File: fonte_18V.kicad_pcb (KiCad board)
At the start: 2 copper layers, 24 parts, among them J1 RJ45_Shielded, Q1 Q_NMOS_GSD, U1 LMR16030

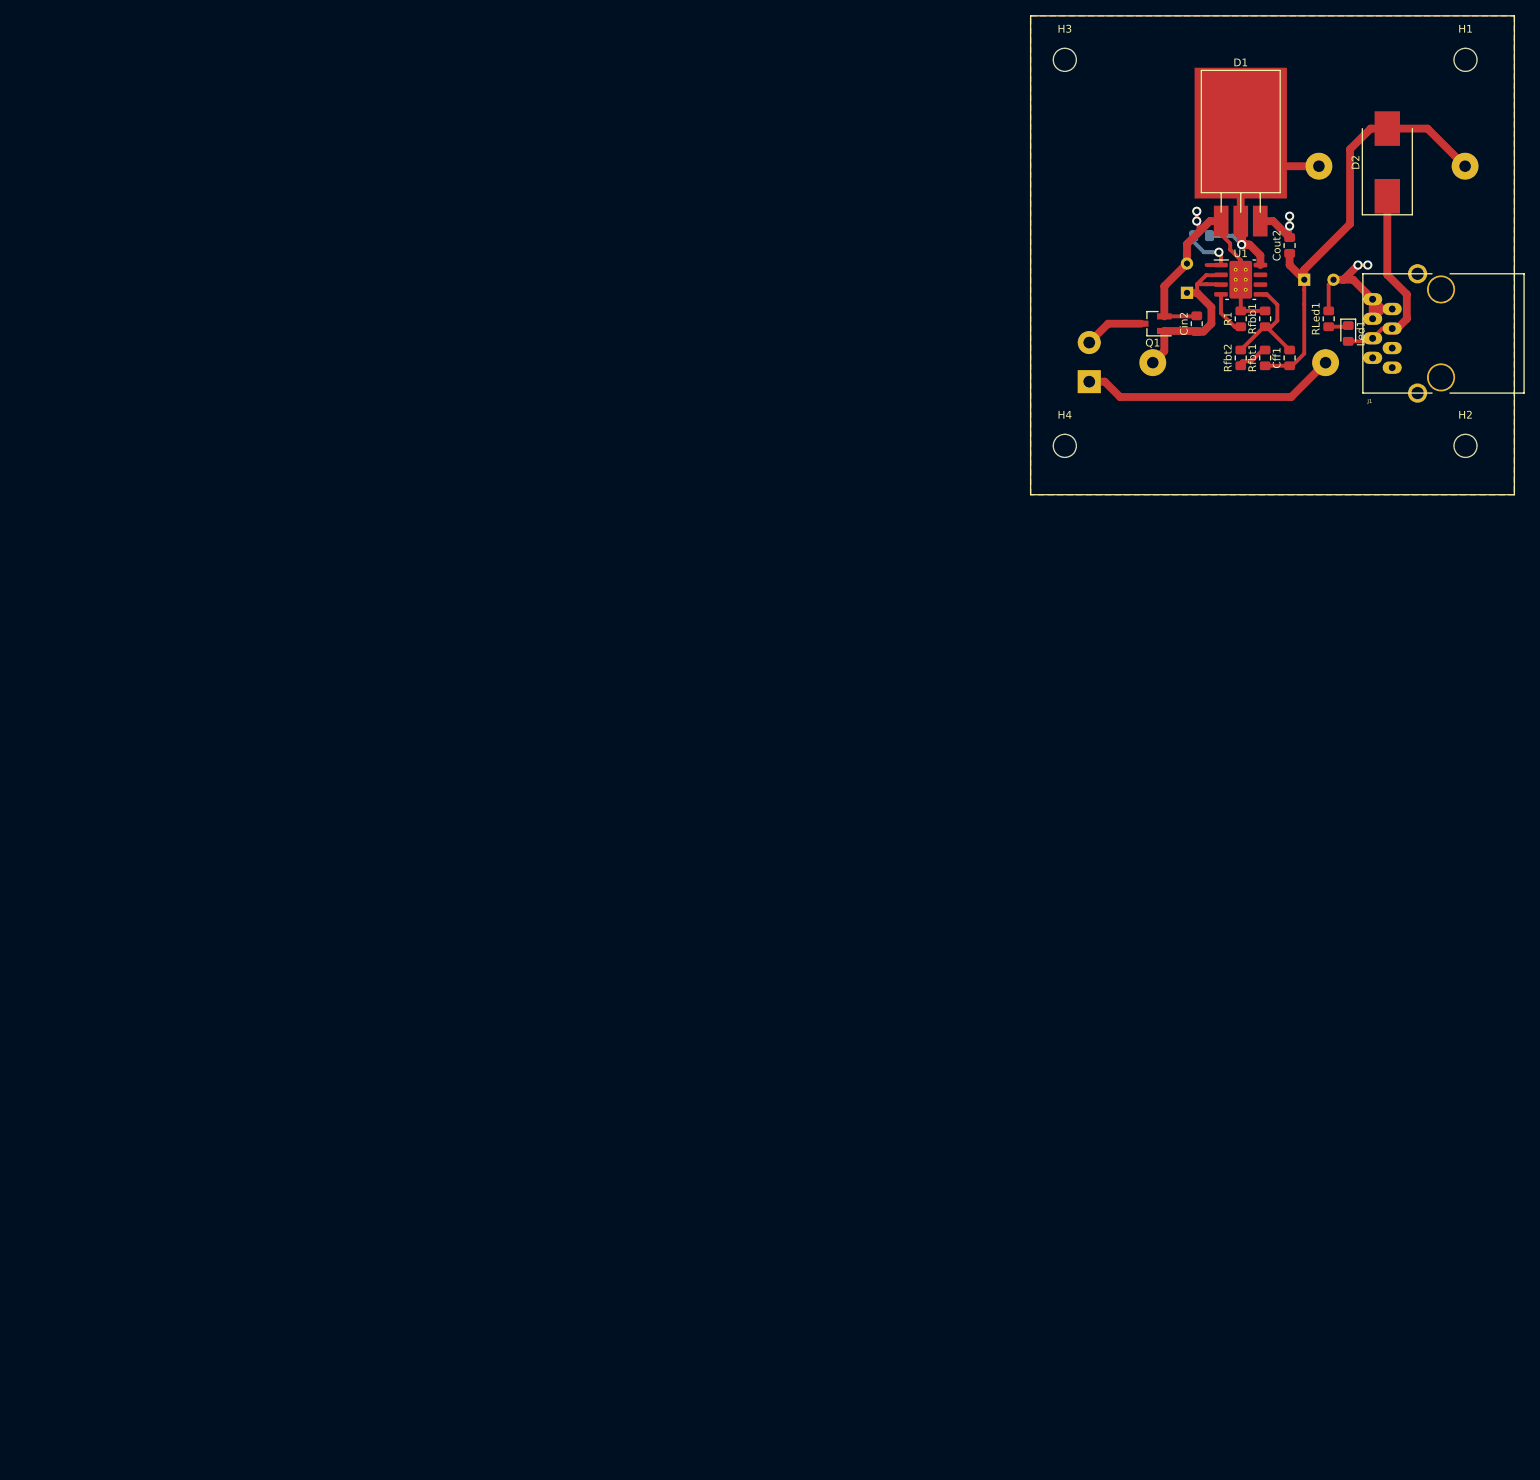
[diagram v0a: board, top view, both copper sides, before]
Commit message: Conectores rj45 adicionados, trilhas melhoradas, acabamentos gerais
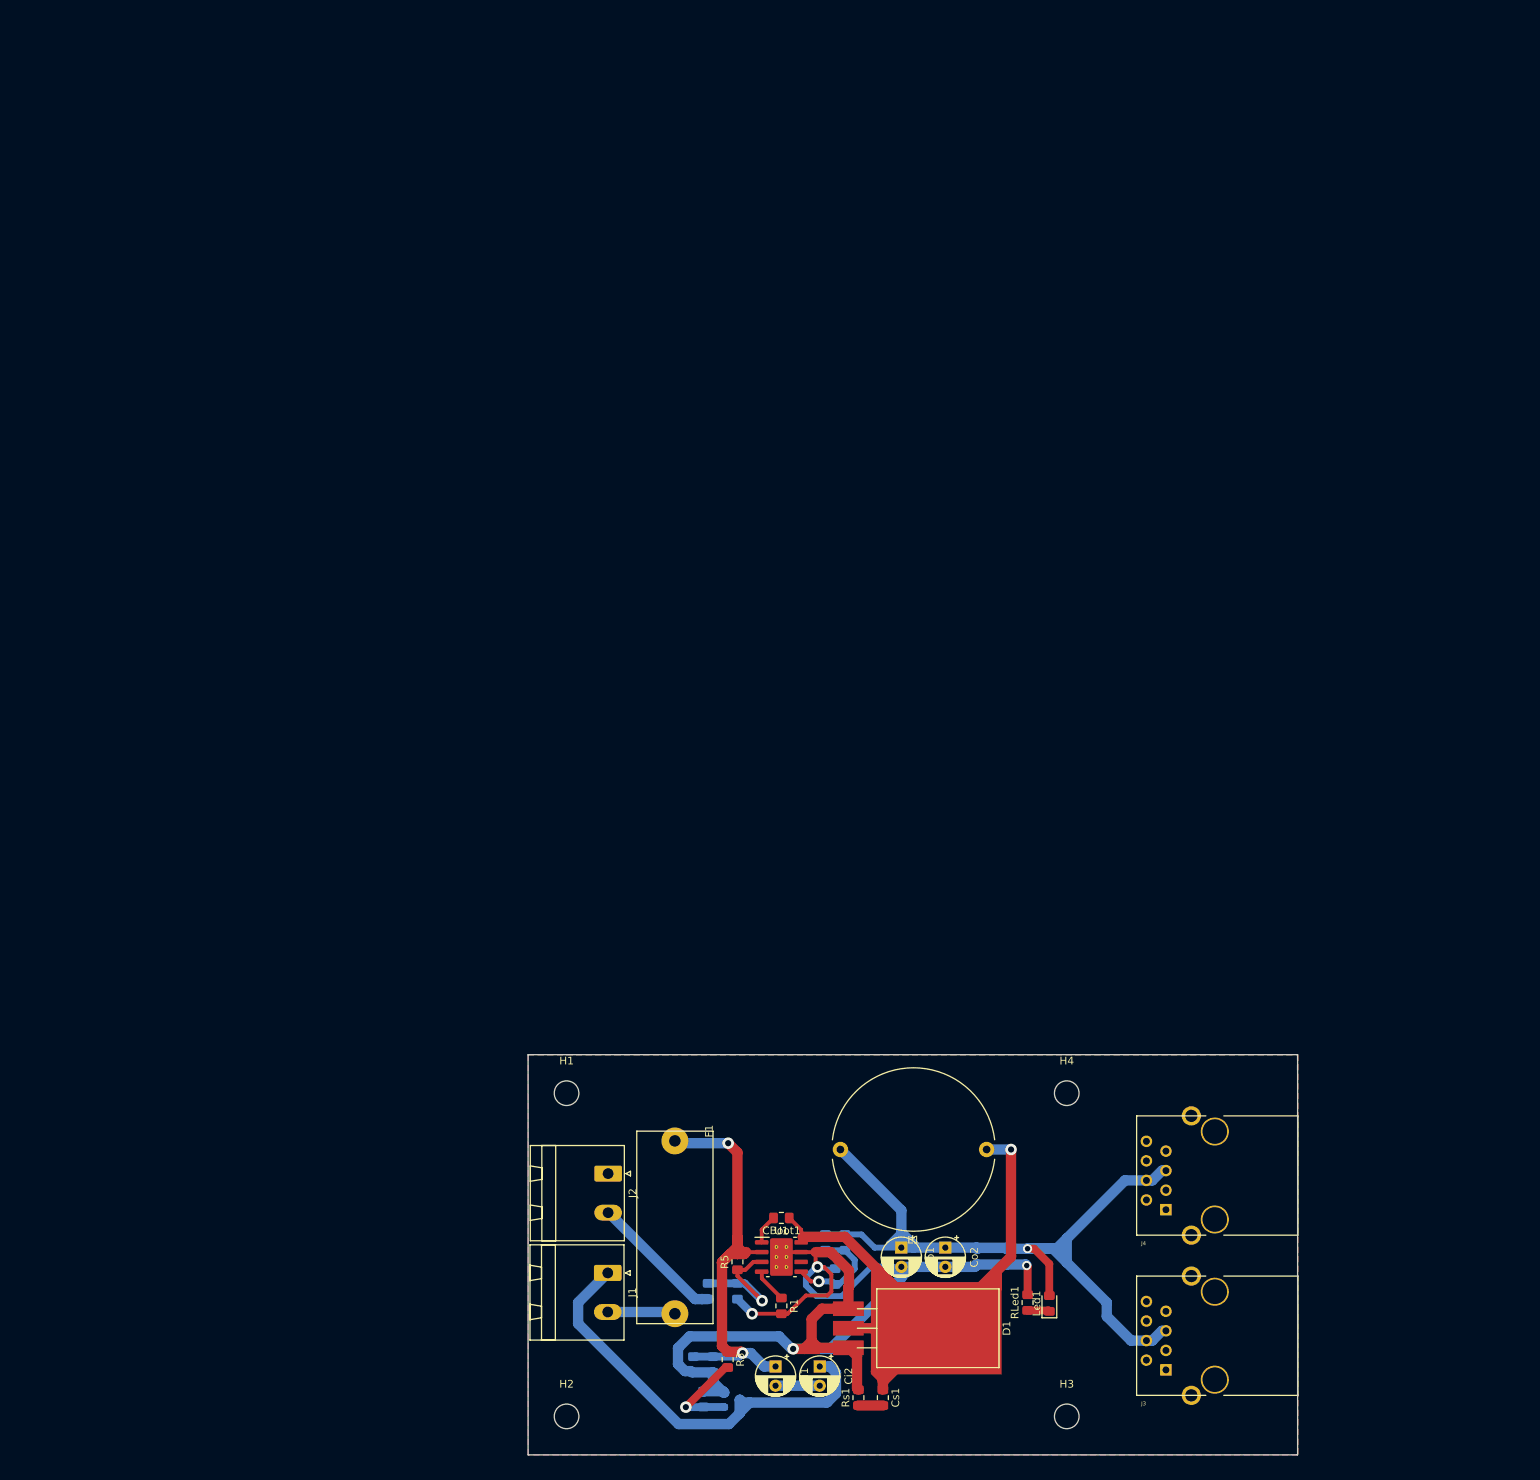
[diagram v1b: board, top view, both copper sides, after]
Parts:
- removed Cin1, Cout1: 100uF, Capacitor_THT:CP_Radial_D8.0mm_P3.80mm
- removed Cout2: 100nF, Capacitor_SMD:C_0805_2012Metric_Pad1.15x1.40mm_HandSolder
- removed D2: SS35, Diode_SMD:D_SMC_Handsoldering
- removed Rfbt1: 5k6, Resistor_SMD:R_0805_2012Metric_Pad1.15x1.40mm_HandSolder
- removed battery1: 21.5<+VBAT<55V1, TerminalBlock:TerminalBlock_bornier-2_P5.08mm
- added Ci1: 10u, Capacitor_THT:CP_Radial_D5.0mm_P2.50mm, F.Cu at (121.2, 175.5)
- added Ci2: 10u, Capacitor_THT:CP_Radial_D5.0mm_P2.50mm, F.Cu at (126.9, 175.5)
- added Cin3: 100nF, Capacitor_SMD:C_0805_2012Metric_Pad1.15x1.40mm_HandSolder, B.Cu at (110.5, 175.3)
- added Co1: 47u, Capacitor_THT:CP_Radial_D5.0mm_P2.50mm, F.Cu at (137.5, 160.1)
- added Co2: 47u, Capacitor_THT:CP_Radial_D5.0mm_P2.50mm, F.Cu at (143.2, 160.1)
- added Co3: o.1u, Capacitor_SMD:C_0805_2012Metric_Pad1.15x1.40mm_HandSolder, B.Cu at (151.2, 161.2)
- added Co4: 0.1u, Capacitor_SMD:C_0805_2012Metric_Pad1.15x1.40mm_HandSolder, B.Cu at (147.4, 161.2)
- added Cs1: 100n, Capacitor_SMD:C_0805_2012Metric_Pad1.15x1.40mm_HandSolder, F.Cu at (135.1, 179.6)
- added J2: MSTBA, Connector_Phoenix_MSTB:PhoenixContact_MSTBA_2,5_2-G-5,08_1x02_P5.08mm_Horizontal, F.Cu at (99.4, 150.4)
- added J3: RJ45_Shielded, MFP19RJ45:RJ45_YH59_01, F.Cu at (171.9, 176.0)
- added J4: RJ45_Shielded, MFP19RJ45:RJ45_YH59_01, F.Cu at (171.9, 155.2)
- added R2: 100, Resistor_SMD:R_0805_2012Metric_Pad1.15x1.40mm_HandSolder, B.Cu at (112.4, 165.7)
- added R3: 220K, Resistor_SMD:R_0805_2012Metric_Pad1.15x1.40mm_HandSolder, F.Cu at (114.9, 174.6)
- added R4: 100K, Resistor_SMD:R_0805_2012Metric_Pad1.15x1.40mm_HandSolder, B.Cu at (111.8, 179.8)
- added R5: 10K, Resistor_SMD:R_0805_2012Metric_Pad1.15x1.40mm_HandSolder, F.Cu at (116.2, 161.9)
- added R6: NA, Resistor_SMD:R_0805_2012Metric_Pad1.15x1.40mm_HandSolder, B.Cu at (116.2, 165.7)
- added Rs1: 2k2, Resistor_SMD:R_0805_2012Metric_Pad1.15x1.40mm_HandSolder, F.Cu at (131.9, 179.6)
- CBoot1, L1: moved to F.Cu
- Cff1: value 33.0pF -> na; moved to B.Cu
- Cin2: moved to B.Cu
- F1: value Fuse -> 2A; moved to F.Cu
- H1, H2, H3, H4: footprint MountingHole:MountingHole_3mm -> MountingHole:MountingHole_3.2mm_M3
- J1: value RJ45_Shielded -> MSTBA; footprint KicadZeniteSolarLibrary18:RJ45_YH59_01 -> Connector_Phoenix_MSTB:PhoenixContact_MSTBA_2,5_2-G-5,08_1x02_P5.08mm_Horizontal
- Q1: value Q_NMOS_GSD -> Si2308CDS; footprint Package_TO_SOT_SMD:SOT-23_Handsoldering -> Package_TO_SOT_SMD:SOT-23; moved to B.Cu
- RLed1: value 750R -> 1k5
- Rfbb1: value 2k2 -> 8k2; moved to B.Cu
- Rfbt2: value 47k -> 230k; moved to B.Cu
- moved H1 178.0 mm to (94.0, 140.0)
- moved H3 176.3 mm to (159.0, 182.0)
- moved H2 171.9 mm to (94.0, 182.0)
- moved J1 155.7 mm to (99.4, 163.4), turned to 270 degrees
- moved Q1 150.2 mm to (115.5, 179.8), turned to 0 degrees
- moved D1 149.4 mm to (130.6, 168.0), turned to 270 degrees
- moved Cin2 149.2 mm to (113.0, 175.3), turned to 270 degrees
- moved R1 141.5 mm to (121.9, 167.6), turned to 270 degrees
- moved U1 140.3 mm to (121.9, 161.3)
- moved CBoot1 138.8 mm to (121.9, 156.2)
- moved Rfbb1 136.4 mm to (128.9, 163.8)
- moved L1 134.9 mm to (148.6, 147.3), turned to 180 degrees
- moved RLed1 133.7 mm to (153.9, 167.2)
- moved Led1 131.9 mm to (156.7, 167.3), turned to 90 degrees
- moved Cff1 128.6 mm to (130.2, 159.4), turned to 270 degrees
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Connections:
- net Net-(Cff1-Pad2) renamed /Feedback
- Cff1 pad 1: Net-(Cff1-Pad1) -> /CAN_18V
- Cin2 pad 1: Net-(Cin1-Pad1) -> Net-(Ci1-Pad1)
- F1 pad 1: Net-(Cin1-Pad1) -> Net-(Ci1-Pad1)
- J1 pad 1: Net-(J1-Pad1) -> Net-(Ci2-Pad1)
- J1 pad 2: Net-(J1-Pad2) -> Net-(F1-Pad2)
- L1 pad 2: Net-(Cff1-Pad1) -> /CAN_18V
- Led1 pad 2: /canbus_connector/CAN_18V -> /CAN_18V
- Q1 pad 1: Net-(Cin1-Pad1) -> Net-(Q1-Pad1)
- Q1 pad 3: Net-(Q1-Pad3) -> Net-(Ci2-Pad1)
- Rfbt2 pad 1: Net-(Rfbt1-Pad2) -> /CAN_18V
- U1 pad 2: Net-(Cin1-Pad1) -> Net-(Ci1-Pad1)
- U1 pad 3: Net-(Cin1-Pad1) -> Net-(R2-Pad1)
- U1 pad 6: Net-(U1-Pad6) -> (no net)
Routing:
- net /CAN_18V: track 0.00 -> 108.7 mm, vias 0 -> 1
- net GND: track 71.4 -> 159.8 mm, vias 6 -> 4
- net Net-(Ci1-Pad1): track 0.00 -> 61.3 mm, vias 0 -> 2
- net Net-(Cff1-Pad1): track 57.7 -> 0.00 mm
- net Net-(CBoot1-Pad1): track 41.2 -> 98.6 mm
- net Net-(Ci2-Pad1): track 0.00 -> 57.2 mm
- net /canbus_connector/CAN_18V: track 25.8 -> 0.00 mm
- net Net-(F1-Pad2): track 33.4 -> 8.81 mm
- net Net-(Cin1-Pad1): track 24.2 -> 0.00 mm
- net Net-(J2-Pad2): track 0.00 -> 17.6 mm
- net Net-(R2-Pad1): track 0.00 -> 16.9 mm, vias 0 -> 1
- net Net-(Q1-Pad1): track 0.00 -> 12.6 mm, vias 0 -> 1
- net Net-(Q1-Pad3): track 7.77 -> 0.00 mm
- net Net-(Ci1-Pad2): track 0.00 -> 5.74 mm
- net Net-(CBoot1-Pad2): track 8.29 -> 3.81 mm, vias 1 -> 0
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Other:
- board outline added: 100 x 52 mm

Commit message: atualizado
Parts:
- moved Cff1 66.6 mm to (63.6, 160.6)
- moved Ci2 66.6 mm to (60.3, 176.7)
- moved Co3 66.6 mm to (84.6, 162.4)
- moved Co4 66.6 mm to (80.8, 162.4)
- moved D1 66.6 mm to (64.0, 169.2)
- moved J2 66.6 mm to (32.8, 151.7)
- moved L1 66.6 mm to (82.0, 148.5)
- moved Led1 66.6 mm to (90.1, 168.5)
- moved Rfbt2 66.6 mm to (61.0, 160.6)
- moved Rs1 66.6 mm to (65.3, 180.8)
- moved CBoot1 66.6 mm to (55.3, 157.4)
- moved Ci1 66.6 mm to (54.6, 176.7)
- moved Cin2 66.6 mm to (46.4, 176.5)
- moved Cin3 66.6 mm to (43.9, 176.5)
- moved Co1 66.6 mm to (70.9, 161.3)
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
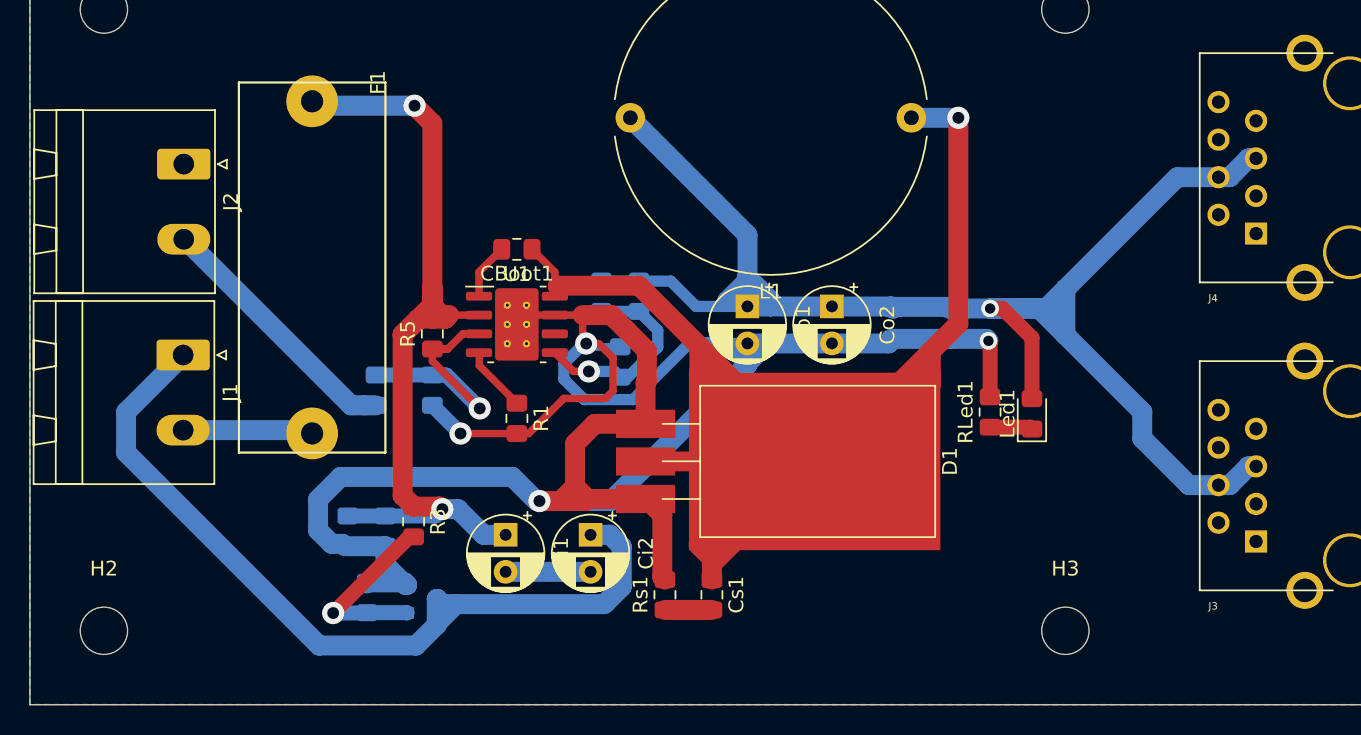
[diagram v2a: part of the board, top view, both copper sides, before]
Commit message: Pads reforçados, algumas pequenas correções de regras
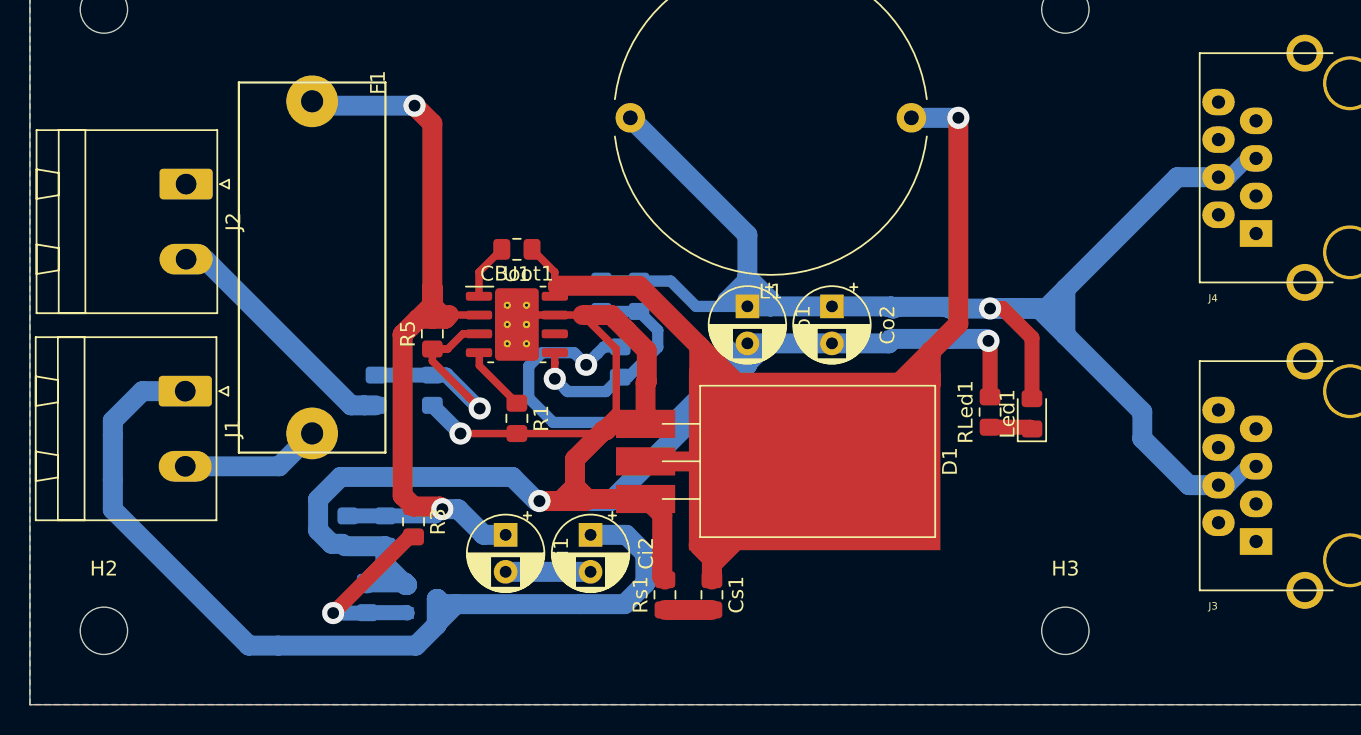
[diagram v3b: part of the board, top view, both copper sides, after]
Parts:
- moved J1 2.45 mm to (32.9, 167.0)
- moved J2 1.36 mm to (33.0, 153.0)
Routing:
- net GND: track 159.8 -> 167.3 mm
- net Net-(Ci2-Pad1): track 57.2 -> 62.8 mm
- net /Feedback: track 14.5 -> 15.8 mm
- net Net-(J2-Pad2): track 17.6 -> 16.9 mm
- net Net-(F1-Pad2): track 8.81 -> 9.50 mm
